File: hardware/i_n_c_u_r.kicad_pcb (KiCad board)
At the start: 2 copper layers, 100 x 100 mm, 38 parts, among them J1 mono_jack_3.5mm, J2 mono_jack_3.5mm, J3 mono_jack_3.5mm, J4 mono_jack_3.5mm, J5 din5, J6 Conn_01x01, J7 rca, J8 2x20_Extra_Tall_Header, U1 MCP3008, U2 6N138

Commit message: update bom
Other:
- board text added: "JLCJLCJLCJLC"

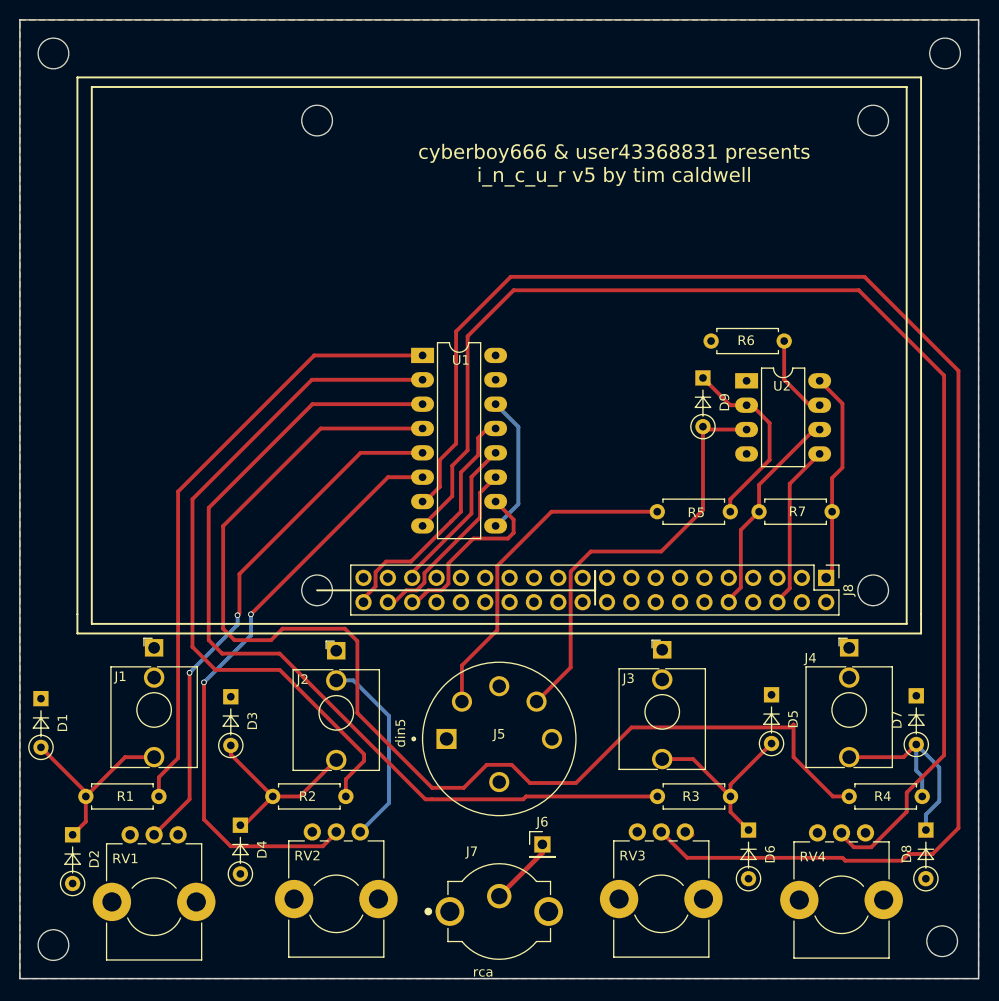
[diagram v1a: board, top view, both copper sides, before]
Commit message: made pot holes bigger - small updates for kicad6
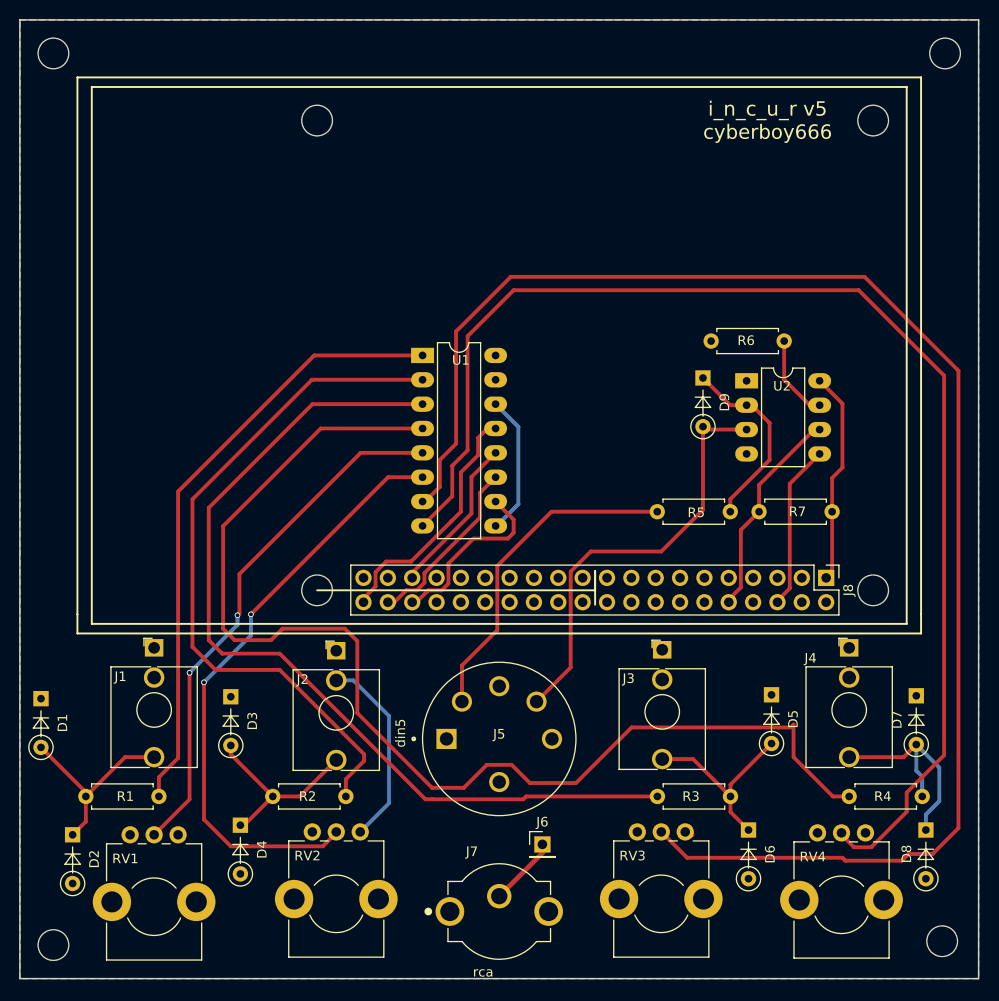
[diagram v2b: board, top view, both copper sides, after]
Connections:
- D5 pad 2: Net-(D5-Pad2) -> Net-(J3-PadT)
- D6 pad 1: Net-(D5-Pad2) -> Net-(J3-PadT)
- J1 pad S: (no net) -> GND
- J1 pad T: (no net) -> Net-(D1-Pad2)
- J1 pad TN: (no net) -> GND
- J2 pad S: (no net) -> GND
- J2 pad T: (no net) -> Net-(D3-Pad2)
- J2 pad TN: (no net) -> GND
- J3 pad S: (no net) -> GND
- J3 pad T: (no net) -> Net-(J3-PadT)
- J3 pad TN: (no net) -> GND
- J4 pad S: (no net) -> GND
- J4 pad T: (no net) -> Net-(D7-Pad2)
- J4 pad TN: (no net) -> GND
- J5 pad 1: Net-(J5-Pad1) -> unconnected-(J5-Pad1)
- J5 pad 2: Net-(J5-Pad2) -> unconnected-(J5-Pad2)
- J5 pad 3: Net-(J5-Pad3) -> unconnected-(J5-Pad3)
- J8 pad 11: Net-(J8-Pad11) -> unconnected-(J8-Pad11)
- J8 pad 12: Net-(J8-Pad12) -> unconnected-(J8-Pad12)
- J8 pad 13: Net-(J8-Pad13) -> unconnected-(J8-Pad13)
- J8 pad 14: Net-(J8-Pad14) -> unconnected-(J8-Pad14)
- J8 pad 15: Net-(J8-Pad15) -> unconnected-(J8-Pad15)
- J8 pad 16: Net-(J8-Pad16) -> unconnected-(J8-Pad16)
- J8 pad 17: Net-(J8-Pad17) -> unconnected-(J8-Pad17)
- J8 pad 18: Net-(J8-Pad18) -> unconnected-(J8-Pad18)
- J8 pad 19: Net-(J8-Pad19) -> unconnected-(J8-Pad19)
- J8 pad 20: Net-(J8-Pad20) -> unconnected-(J8-Pad20)
- J8 pad 21: Net-(J8-Pad21) -> unconnected-(J8-Pad21)
- J8 pad 22: Net-(J8-Pad22) -> unconnected-(J8-Pad22)
- J8 pad 23: Net-(J8-Pad23) -> unconnected-(J8-Pad23)
- J8 pad 24: Net-(J8-Pad24) -> unconnected-(J8-Pad24)
- J8 pad 25: Net-(J8-Pad25) -> unconnected-(J8-Pad25)
- J8 pad 26: Net-(J8-Pad26) -> unconnected-(J8-Pad26)
- J8 pad 27: Net-(J8-Pad27) -> unconnected-(J8-Pad27)
- J8 pad 28: Net-(J8-Pad28) -> unconnected-(J8-Pad28)
- J8 pad 29: Net-(J8-Pad29) -> unconnected-(J8-Pad29)
- J8 pad 3: Net-(J8-Pad3) -> unconnected-(J8-Pad3)
- J8 pad 30: Net-(J8-Pad30) -> unconnected-(J8-Pad30)
- J8 pad 31: Net-(J8-Pad31) -> unconnected-(J8-Pad31)
- J8 pad 32: Net-(J8-Pad32) -> unconnected-(J8-Pad32)
- J8 pad 33: Net-(J8-Pad33) -> unconnected-(J8-Pad33)
- J8 pad 34: Net-(J8-Pad34) -> unconnected-(J8-Pad34)
- J8 pad 37: Net-(J8-Pad37) -> unconnected-(J8-Pad37)
- J8 pad 39: Net-(J8-Pad39) -> unconnected-(J8-Pad39)
- J8 pad 4: Net-(J8-Pad4) -> unconnected-(J8-Pad4)
- J8 pad 5: Net-(J8-Pad5) -> unconnected-(J8-Pad5)
- J8 pad 7: Net-(J8-Pad7) -> unconnected-(J8-Pad7)
- J8 pad 8: Net-(J8-Pad8) -> unconnected-(J8-Pad8)
- J8 pad 9: Net-(J8-Pad9) -> unconnected-(J8-Pad9)
- R3 pad 2: Net-(D5-Pad2) -> Net-(J3-PadT)
- U2 pad 1: Net-(U2-Pad1) -> unconnected-(U2-Pad1)
- U2 pad 4: Net-(U2-Pad4) -> unconnected-(U2-Pad4)
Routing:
- net Net-(J3-PadT): track 0.00 -> 20.3 mm
- net Net-(D5-Pad2): track 20.3 -> 0.00 mm
- net unconnected-(J5-Pad2): track 0.00 -> 0.75 mm
- net Net-(J5-Pad2): track 0.75 -> 0.00 mm
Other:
- net class Default removed
- board text added: "i_n_c_u_r v5 cyberboy666"
- board text removed: "cyberboy666 & user43368831 presents i_n_c_u_r v5 by tim caldwell"
